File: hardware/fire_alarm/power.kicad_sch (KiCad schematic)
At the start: 17 parts, among them J1 Barrel_Jack_Switch, U1 MP1584EN-LF-Z, U2 MCP1700x-330xxTT

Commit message: feat: update power mcu
Signed-off-by: Trung Hieu Nguyen <hieu.nguyenarc03@gmail.com>
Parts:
- C1: value 10uF 50V -> 10uF 25V; footprint Capacitor_SMD:C_0805_2012Metric_Pad1.18x1.45mm_HandSolder -> Capacitor_SMD:C_0603_1608Metric_Pad1.08x0.95mm_HandSolder
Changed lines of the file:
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@@
 		(on_board yes)
 		(dnp no)
-		(fields_autoplaced yes)
 		(property "Reference" "C1"
 			(at 96.52 69.8499 0)
@@
 			)
 		)
-		(property "Value" "10uF 50V"
-			(at 96.52 72.3899 0)
+		(property "Value" "10uF 25V"
+			(at 89.154 72.136 0)
 			(effects
 				(font
@@
 			)
 		)
-		(property "Footprint" "Capacitor_SMD:C_0805_2012Metric_Pad1.18x1.45mm_HandSolder"
+		(property "Footprint" "Capacitor_SMD:C_0603_1608Metric_Pad1.08x0.95mm_HandSolder"
 			(at 93.6752 74.93 0)
 			(effects
@@
 		(on_board yes)
 		(dnp no)
-		(fields_autoplaced yes)
 		(property "Reference" "R1"
 			(at 107.95 69.8499 0)
@@
 		)
 		(property "Value" "100kOhm 0.1W"
-			(at 107.95 72.3899 0)
+			(at 101.6 73.152 0)
 			(effects
 				(font
@@
 		)
 		(property "Value" "24.9kOhm 0.125W"
-			(at 203.2 75.184 0)
+			(at 197.358 71.882 0)
 			(effects
 				(font
@@
 		)
 		(property "Value" "42.2kOhm 0.1W"
-			(at 171.45 72.3899 0)
-			(effects
-				(font
+			(at 161.29 72.39 0)
+			(effects
+				(font

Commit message: feat: continue laying out schematic MCU
Signed-off-by: Trung Hieu Nguyen <hieu.nguyenarc03@gmail.com>
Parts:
- added C10: 470uF 16V, Capacitor_SMD:CP_Elec_8x10.5, symbol Device:C_Polarized
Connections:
- net +3.3V: now also C10.1
- net GND: now also C10.2
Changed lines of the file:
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@@
+	)
+	(junction
+		(at 182.88 123.19)
+		(diameter 0)
+		(color 0 0 0 0)
 	)
 	(junction
@@
 	)
 	(junction
+		(at 162.56 123.19)
+		(diameter 0)
+		(color 0 0 0 0)
+	)
+	(junction
 		(at 100.33 58.42)
 		(diameter 0)
@@
 	)
 	(junction
-		(at 162.56 123.19)
-		(diameter 0)
-		(color 0 0 0 0)
-	)
-	(junction
 		(at 198.12 55.88)
 		(diameter 0)
@@
 	(wire
 		(pts
+			(xy 182.88 123.19) (xy 182.88 132.08)
+		)
+		(stroke
+			(width 0)
+			(type default)
+		)
+	)
+	(wire
+		(pts
 			(xy 113.03 38.1) (xy 138.43 38.1)
 		)
@@
 	(wire
 		(pts
+			(xy 198.12 115.57) (xy 198.12 123.19)
+		)
+		(stroke
+			(width 0)
+			(type default)
+		)
+	)
+	(wire
+		(pts
+			(xy 198.12 123.19) (xy 182.88 123.19)
+		)
+		(stroke
+			(width 0)
+			(type default)
+		)
+	)
+	(wire
+		(pts
 			(xy 190.5 58.42) (xy 190.5 67.31)
 		)
@@
 	(wire
 		(pts
-			(xy 175.26 123.19) (xy 162.56 123.19)
-		)
-		(stroke
-			(width 0)
-			(type default)
-		)
-	)
-	(wire
-		(pts
 			(xy 100.33 29.21) (xy 100.33 58.42)
 		)
@@
 	(wire
 		(pts
+			(xy 162.56 123.19) (xy 182.88 123.19)
+		)
+		(stroke
+			(width 0)
+			(type default)
+		)
+	)
+	(wire
+		(pts
 			(xy 113.03 55.88) (xy 113.03 38.1)
 		)
@@
 	(wire
 		(pts
+			(xy 182.88 139.7) (xy 182.88 144.78)
+		)
+		(stroke
+			(width 0)
+			(type default)
+		)
+	)
+	(wire
+		(pts
 			(xy 100.33 58.42) (xy 121.92 58.42)
 		)
@@
 		(pts
 			(xy 118.11 63.5) (xy 118.11 83.82)
-		)
-		(stroke
-			(width 0)
-			(type default)
-		)
-	)
-	(wire
-		(pts
-			(xy 175.26 115.57) (xy 175.26 123.19)
 		)
 		(stroke
@@
 	(symbol
 		(lib_id "power:+3.3V")
-		(at 175.26 115.57 0)
+		(at 198.12 115.57 0)
 		(unit 1)
 		(exclude_from_sim no)
@@
 		(fields_autoplaced yes)
 		(property "Reference" "#PWR015"
-			(at 175.26 119.38 0)
+			(at 198.12 119.38 0)
 			(effects
 				(font
@@
 		)
 		(property "Value" "+3.3V"
-			(at 175.26 110.49 0)
+			(at 198.12 110.49 0)
 			(effects
 				(font
@@
 		)
 		(property "Footprint" ""
-			(at 175.26 115.57 0)
+			(at 198.12 115.57 0)
 			(effects
 				(font
@@
 		)
 		(property "Datasheet" ""
-			(at 175.26 115.57 0)
+			(at 198.12 115.57 0)
 			(effects
 				(font
@@
 		)
 		(property "Description" "Power symbol creates a global label with name \"+3.3V\""
-			(at 175.26 115.57 0)
+			(at 198.12 115.57 0)
 			(effects
 				(font
@@
 	)
 	(symbol
+		(lib_id "power:GND")
+		(at 182.88 144.78 0)
+		(unit 1)
+		(exclude_from_sim no)
+		(in_bom yes)
+		(on_board yes)
+		(dnp no)
+		(fields_autoplaced yes)
+		(property "Reference" "#PWR021"
+			(at 182.88 151.13 0)
+			(effects
+				(font
+					(size 1.27 1.27)
+				)
+				(hide yes)
+			)
+		)
+		(property "Value" "GND"
+			(at 182.88 149.86 0)
+			(effects
+				(font
+					(size 1.27 1.27)
+				)
+			)
+		)
+		(property "Footprint" ""
+			(at 182.88 144.78 0)
+			(effects
+				(font
+					(size 1.27 1.27)
+				)
+				(hide yes)
+			)
+		)
+		(property "Datasheet" ""
+			(at 182.88 144.78 0)
+			(effects
+				(font
+					(size 1.27 1.27)
+				)
+				(hide yes)
+			)
+		)
+		(property "Description" "Power symbol creates a global label with name \"GND\" , ground"
+			(at 182.88 144.78 0)
+			(effects
+				(font
+					(size 1.27 1.27)
+				)
+				(hide yes)
+			)
+		)
+		(pin "1"
+		)
+		(instances
+			(project "fire_alarm"
+				(path "/0ad2965f-ac4e-45fe-9d64-44da87c25aaa/e71bccc5-6439-4fb2-9a3d-1d241e0de8c1"
+					(reference "#PWR021")
+					(unit 1)
+				)
+			)
+		)
+	)
+	(symbol
 		(lib_id "Device:D_Schottky")
 		(at 217.17 71.12 270)
@@
 					(unit 1)
 				)
+			)
+		)
+	)
+	(symbol
+		(lib_id "Device:C_Polarized")
+		(at 182.88 135.89 0)
+		(unit 1)
+		(exclude_from_sim no)
+		(in_bom yes)
+		(on_board yes)
+		(dnp no)
+		(fields_autoplaced yes)
+		(property "Reference" "C10"
+			(at 186.69 133.7309 0)
+			(effects
+				(font
+					(size 1.27 1.27)
+				)
+				(justify left)
+			)
+		)
+		(property "Value" "470uF 16V"
+			(at 186.69 136.2709 0)
+			(effects
+				(font
+					(size 1.27 1.27)
+				)
+				(justify left)
+			)
+		)
+		(property "Footprint" "Capacitor_SMD:CP_Elec_8x10.5"
+			(at 183.8452 139.7 0)
+			(effects
+				(font
+					(size 1.27 1.27)
+				)
+				(hide yes)
+			)
+		)
+		(property "Datasheet" "~"
+			(at 182.88 135.89 0)
+			(effects
+				(font
+					(size 1.27 1.27)
+				)
+				(hide yes)
+			)
+		)
+		(property "Description" "Polarized capacitor"
+			(at 182.88 135.89 0)
+			(effects
+				(font
+					(size 1.27 1.27)
+				)
+				(hide yes)
+			)
+		)
+		(pin "1"
+		)
+		(pin "2"
+		)
+		(instances
+			(project ""
+				(path "/0ad2965f-ac4e-45fe-9d64-44da87c25aaa/e71bccc5-6439-4fb2-9a3d-1d241e0de8c1"
+					(reference "C10")
+					(unit 1)
+				)

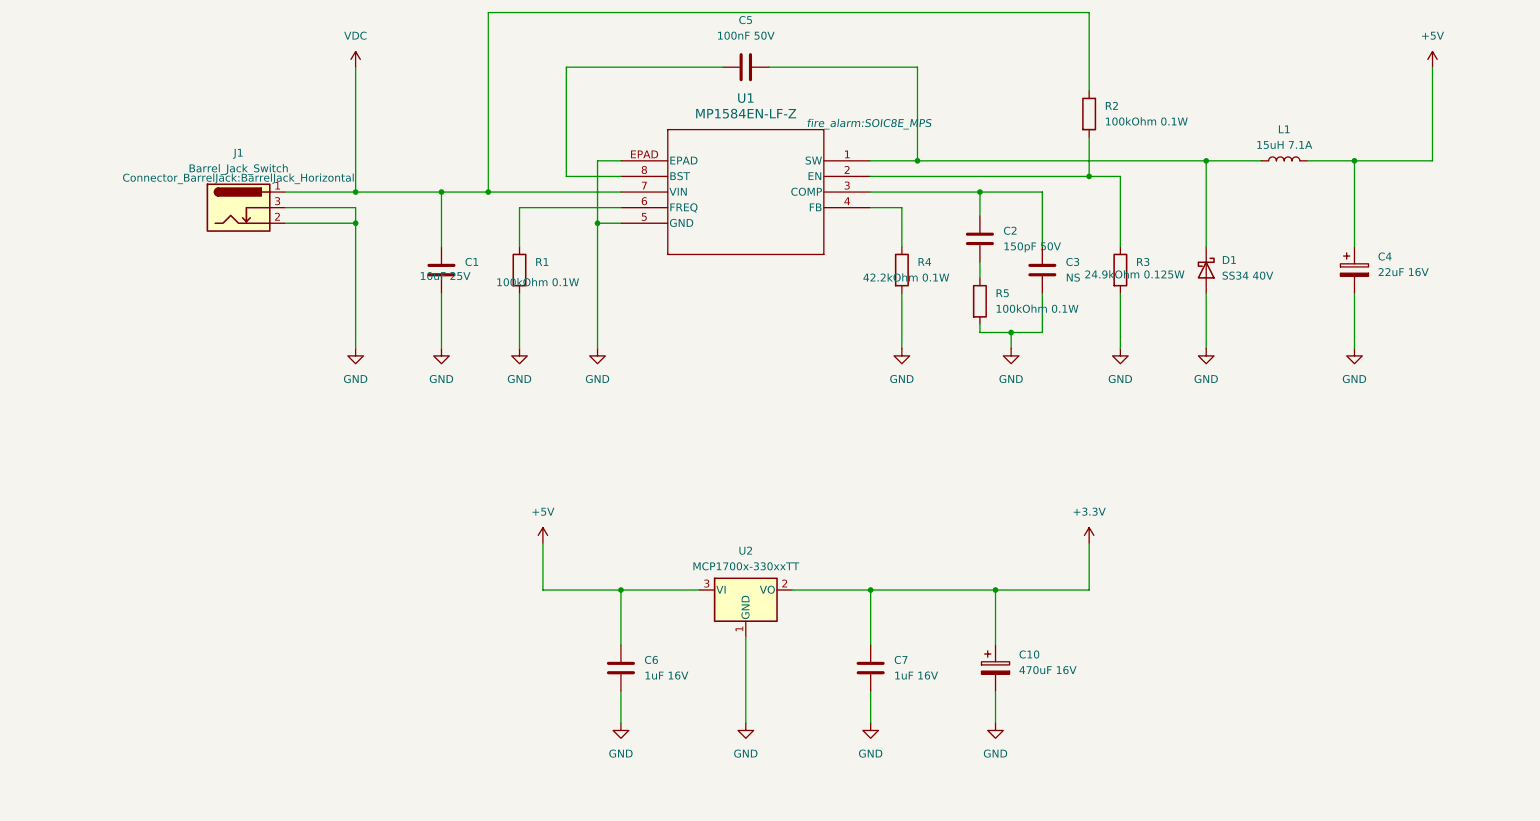
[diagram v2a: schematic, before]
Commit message: feat: update schematic sensors, ui
Signed-off-by: Trung Hieu Nguyen <hieu.nguyenarc03@gmail.com>
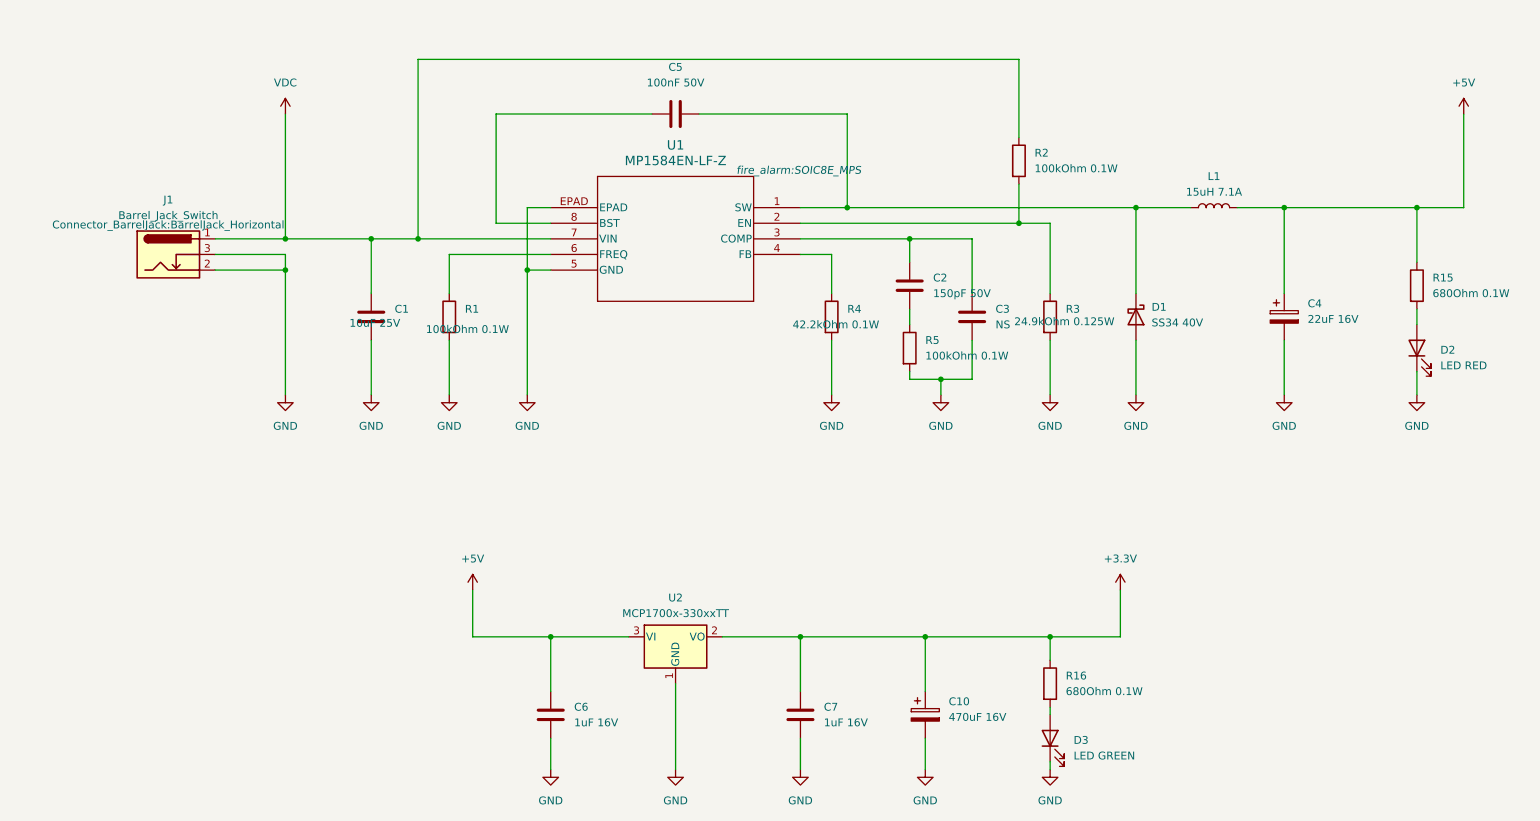
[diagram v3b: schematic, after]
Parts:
- added D2: LED RED, LED_SMD:LED_0805_2012Metric_Pad1.15x1.40mm_HandSolder, symbol Device:LED
- added D3: LED GREEN, LED_SMD:LED_0805_2012Metric_Pad1.15x1.40mm_HandSolder, symbol Device:LED
- added R15, R16: 680Ohm 0.1W, Resistor_SMD:R_0603_1608Metric_Pad0.98x0.95mm_HandSolder, symbol Device:R
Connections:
- net +3.3V: now also R16.1
- net +5V: now also R15.1
- net GND: now also D2.1 (K), D3.1 (K)
- new net: D2.2 (A), R15.2
- new net: D3.2 (A), R16.2
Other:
- moved on the sheet: C1, C10, C2, C3, C4, C5, C6, C7, D1, J1, L1, R1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
